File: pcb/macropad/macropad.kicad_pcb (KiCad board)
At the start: 2 copper layers, 39.5 x 62 mm, 8 parts, among them SW1 SW_Push, SW2 SW_Push, SW3 SW_Push, SW4 SW_Push, U1 XIAO-RP2040-DIP

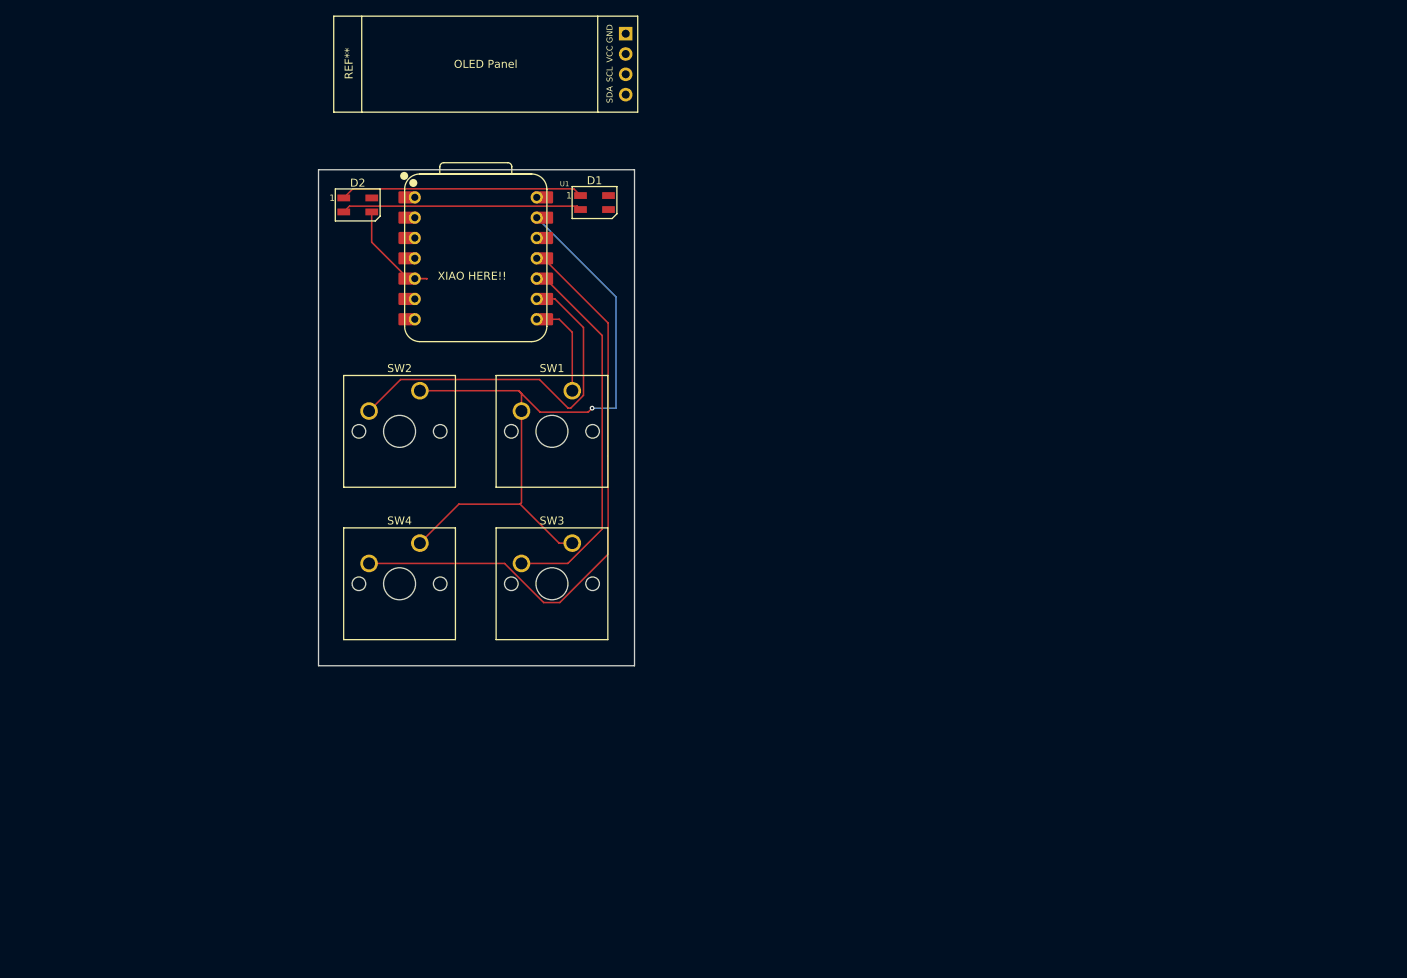
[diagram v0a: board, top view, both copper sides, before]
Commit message: changes to the pcb, case changes will follow
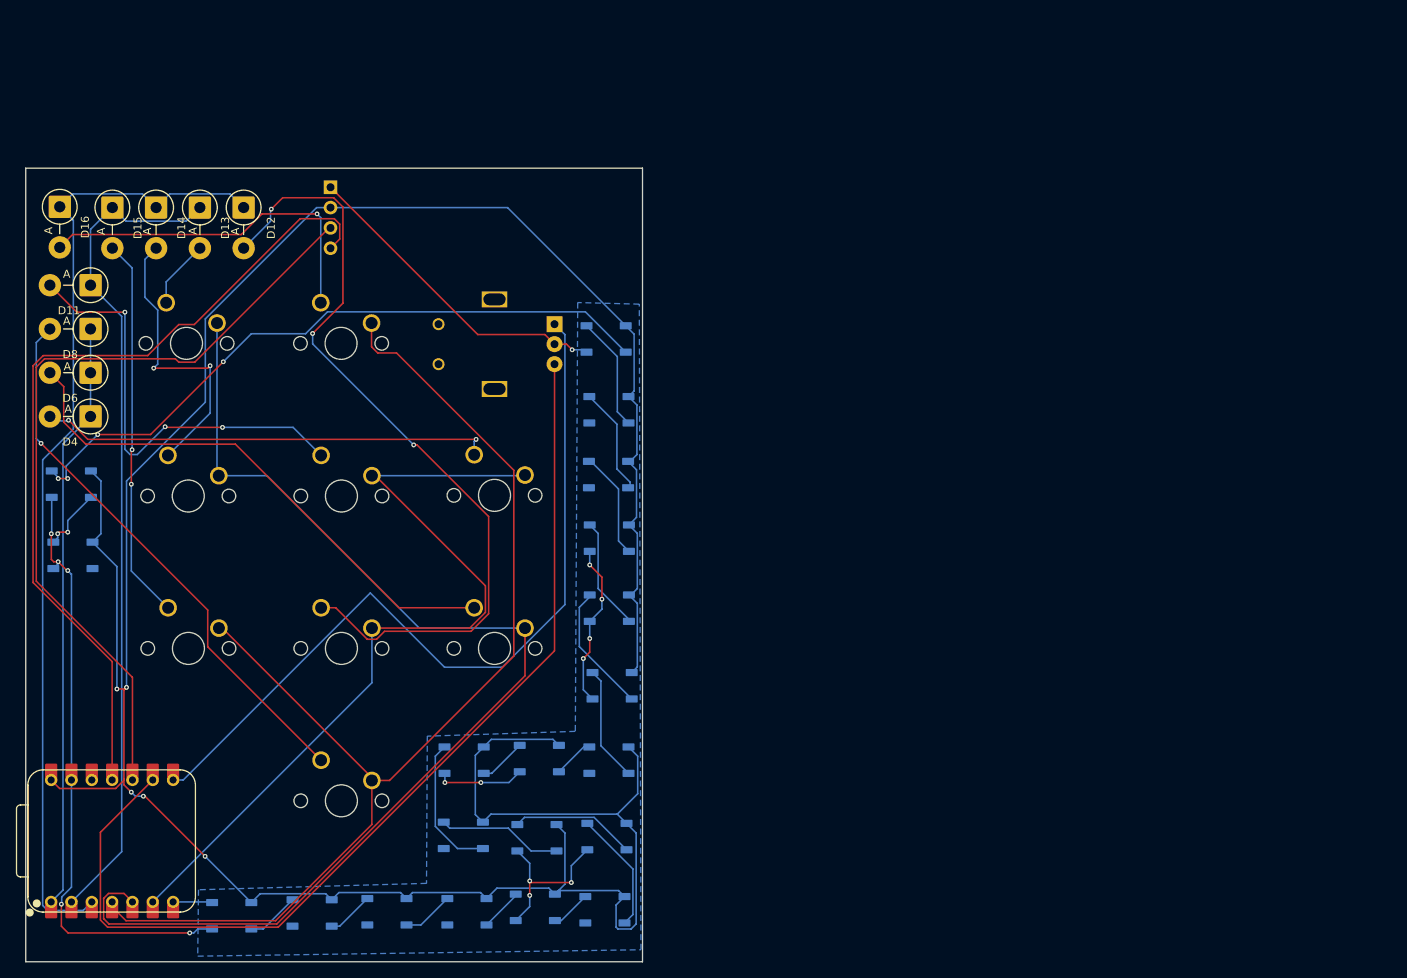
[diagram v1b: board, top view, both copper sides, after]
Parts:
- removed REF**: SSD1306-0.91-OLED-4pin-128x32, Downloads:SSD1306-0.91-OLED-4pin-128x32
- removed SW1, SW2, SW3: SW_Push, Button_Switch_Keyboard:SW_Cherry_MX_1.00u_PCB
- added D10: WS2812B, LED_SMD:LED_WS2812B_PLCC4_5.0x5.0mm_P3.2mm, B.Cu at (152.2, 110.0)
- added D11: D_Small, Diode_THT:D_5W_P5.08mm_Vertical_AnodeUp, F.Cu at (87.3, 69.6)
- added D12: D_Small, Diode_THT:D_5W_P5.08mm_Vertical_AnodeUp, F.Cu at (106.4, 59.9)
- added D13: D_Small, Diode_THT:D_5W_P5.08mm_Vertical_AnodeUp, F.Cu at (101.0, 59.9)
- added D14: D_Small, Diode_THT:D_5W_P5.08mm_Vertical_AnodeUp, F.Cu at (95.5, 59.9)
- added D15: D_Small, Diode_THT:D_5W_P5.08mm_Vertical_AnodeUp, F.Cu at (90.0, 59.9)
- added D16: D_Small, Diode_THT:D_5W_P5.08mm_Vertical_AnodeUp, F.Cu at (83.5, 59.8)
- added D17: WS2812B, LED_SMD:LED_WS2812B_PLCC4_5.0x5.0mm_P3.2mm, B.Cu at (152.2, 101.2)
- added D18: WS2812B, LED_SMD:LED_WS2812B_PLCC4_5.0x5.0mm_P3.2mm, B.Cu at (151.6, 147.7)
- added D19: WS2812B, LED_SMD:LED_WS2812B_PLCC4_5.0x5.0mm_P3.2mm, B.Cu at (152.1, 93.3)
- added D20: WS2812B, LED_SMD:LED_WS2812B_PLCC4_5.0x5.0mm_P3.2mm, B.Cu at (151.8, 138.6)
- added D21: WS2812B, LED_SMD:LED_WS2812B_PLCC4_5.0x5.0mm_P3.2mm, B.Cu at (152.1, 85.2)
- added D22: WS2812B, LED_SMD:LED_WS2812B_PLCC4_5.0x5.0mm_P3.2mm, B.Cu at (143.1, 138.7)
- added D23: WS2812B, LED_SMD:LED_WS2812B_PLCC4_5.0x5.0mm_P3.2mm, B.Cu at (151.8, 76.3)
- added D24: WS2812B, LED_SMD:LED_WS2812B_PLCC4_5.0x5.0mm_P3.2mm, B.Cu at (133.9, 138.4)
- added D25: WS2812B, LED_SMD:LED_WS2812B_PLCC4_5.0x5.0mm_P3.2mm, B.Cu at (84.9, 94.5)
- added D26: WS2812B, LED_SMD:LED_WS2812B_PLCC4_5.0x5.0mm_P3.2mm, B.Cu at (134.0, 129.0)
- added D27: WS2812B, LED_SMD:LED_WS2812B_PLCC4_5.0x5.0mm_P3.2mm, B.Cu at (143.4, 128.8)
- added D28: WS2812B, LED_SMD:LED_WS2812B_PLCC4_5.0x5.0mm_P3.2mm, B.Cu at (85.1, 103.4)
- added D29: WS2812B, LED_SMD:LED_WS2812B_PLCC4_5.0x5.0mm_P3.2mm, B.Cu at (105.0, 148.4)
- added D3: WS2812B, LED_SMD:LED_WS2812B_PLCC4_5.0x5.0mm_P3.2mm, B.Cu at (134.3, 147.9)
- added D4: D_Small, Diode_THT:D_5W_P5.08mm_Vertical_AnodeUp, F.Cu at (87.3, 86.0)
- added D5: WS2812B, LED_SMD:LED_WS2812B_PLCC4_5.0x5.0mm_P3.2mm, B.Cu at (142.9, 147.4)
- added D6: D_Small, Diode_THT:D_5W_P5.08mm_Vertical_AnodeUp, F.Cu at (87.3, 80.6)
- added D7: WS2812B, LED_SMD:LED_WS2812B_PLCC4_5.0x5.0mm_P3.2mm, B.Cu at (152.1, 129.0)
- added D8: D_Small, Diode_THT:D_5W_P5.08mm_Vertical_AnodeUp, F.Cu at (87.3, 75.1)
- added D9: WS2812B, LED_SMD:LED_WS2812B_PLCC4_5.0x5.0mm_P3.2mm, B.Cu at (152.5, 119.7)
- added OLED1: ~, Downloads:SSD1306-0.91-OLED-4pin-128x32, B.Cu at (153.8, 55.2)
- added SW11: SW_Push, Button_Switch_Keyboard:SW_Cherry_MX_1.00u_PCB, B.Cu at (116.1, 90.9)
- added SW12: SW_Push, Button_Switch_Keyboard:SW_Cherry_MX_1.00u_PCB, B.Cu at (116.1, 110.0)
- added SW13: SW_Push, Button_Switch_Keyboard:SW_Cherry_MX_1.00u_PCB, B.Cu at (96.8, 71.8)
- added SW14: SW_Push, Button_Switch_Keyboard:SW_Cherry_MX_1.00u_PCB, B.Cu at (97.0, 90.9)
- added SW15: SW_Push, Button_Switch_Keyboard:SW_Cherry_MX_1.00u_PCB, B.Cu at (97.0, 110.0)
- added SW16: SW_Push, Button_Switch_Keyboard:SW_Cherry_MX_1.00u_PCB, B.Cu at (116.1, 71.8)
- added SW17: RotaryEncoder, Downloads:RotaryEncoder_Alps_EC11E_Vertical_H20mm, B.Cu at (145.3, 74.5)
- added SW6: SW_Push, Button_Switch_Keyboard:SW_Cherry_MX_1.00u_PCB, B.Cu at (135.3, 110.0)
- added SW8: SW_Push, Button_Switch_Keyboard:SW_Cherry_MX_1.00u_PCB, B.Cu at (116.1, 129.0)
- D1, D2: value SK6812MINI -> WS2812B; footprint LED_SMD:LED_SK6812MINI_PLCC4_3.5x3.5mm_P1.75mm -> LED_SMD:LED_WS2812B_PLCC4_5.0x5.0mm_P3.2mm; moved to B.Cu
- SW4: moved to B.Cu
- moved D1 95.6 mm to (115.0, 148.1), turned to 180 degrees
- moved D2 88.4 mm to (124.3, 147.9), turned to 180 degrees
- moved U1 85.9 mm to (90.0, 139.1), turned to 90 degrees
- moved SW4 13.0 mm to (135.3, 90.8), turned to 180 degrees
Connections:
- D1 pad 1: Net-(D1-DOUT) -> VCC
- D1 pad 2: Net-(D1-VSS) -> Net-(D1-DOUT)
- D1 pad 3: unconnected-(D1-DIN-Pad3) -> GND
- D1 pad 4: +5V -> Net-(D1-DIN)
- D2 pad 1: Net-(D1-DOUT) -> VCC
- D2 pad 2: Net-(D1-VSS) -> Net-(D2-DOUT)
- D2 pad 3: Net-(D2-DIN) -> GND
- D2 pad 4: +5V -> Net-(D1-DOUT)
- SW4 pad 1: GND -> Net-(D4-A)
- SW4 pad 2: Net-(U1-GPIO3/MOSI) -> COL2
- U1 pad 1: unconnected-(U1-GPIO26/ADC0/A0-Pad1) -> ROW0
- U1 pad 11: Net-(U1-GPIO3/MOSI) -> Net-(OLED1-SDA)
- U1 pad 14: +5V -> VCC
- U1 pad 2: unconnected-(U1-GPIO27/ADC1/A1-Pad2) -> ROW1
- U1 pad 3: unconnected-(U1-GPIO28/ADC2/A2-Pad3) -> ROW2
- U1 pad 4: unconnected-(U1-GPIO29/ADC3/A3-Pad4) -> COL0
- U1 pad 5: Net-(D2-DIN) -> COL1
- U1 pad 6: unconnected-(U1-GPIO7/SCL-Pad6) -> COL2
- U1 pad 7: unconnected-(U1-GPIO0/TX-Pad7) -> Net-(D29-DIN)
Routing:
- net VCC: track 0.00 -> 365.9 mm, vias 0 -> 5
- net COL0: track 0.00 -> 146.1 mm
- net COL1: track 0.00 -> 143.9 mm
- net ROW2: track 0.00 -> 122.2 mm
- net Net-(OLED1-SDA): track 0.00 -> 105.6 mm
- net ROW1: track 0.00 -> 104.5 mm
- net COL2: track 0.00 -> 103.0 mm
- net Net-(D12-A): track 0.00 -> 102.2 mm, vias 0 -> 3
- net Net-(U1-GPIO1/RX): track 12.4 -> 101.3 mm
- net Net-(D23-DOUT): track 0.00 -> 84.1 mm, vias 0 -> 4
- net Net-(U1-GPIO2/SCK): track 46.4 -> 127.5 mm
- net GND: track 91.5 -> 168.5 mm, vias 1 -> 15
- net Net-(U1-GPIO3/MOSI): track 75.6 -> 0.00 mm
- net ROW0: track 0.00 -> 73.7 mm
- net Net-(D8-A): track 0.00 -> 69.4 mm, vias 0 -> 1
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- added copper zone on B.Cu, net GND
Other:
- board size 39.5 x 62 mm -> 77.1 x 99.2 mm
- board text removed: "Itay Zimet's Hackpad"
- board text removed: "XIAO HERE!!"

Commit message: remade pcb
removed leds and better wiring (much better)
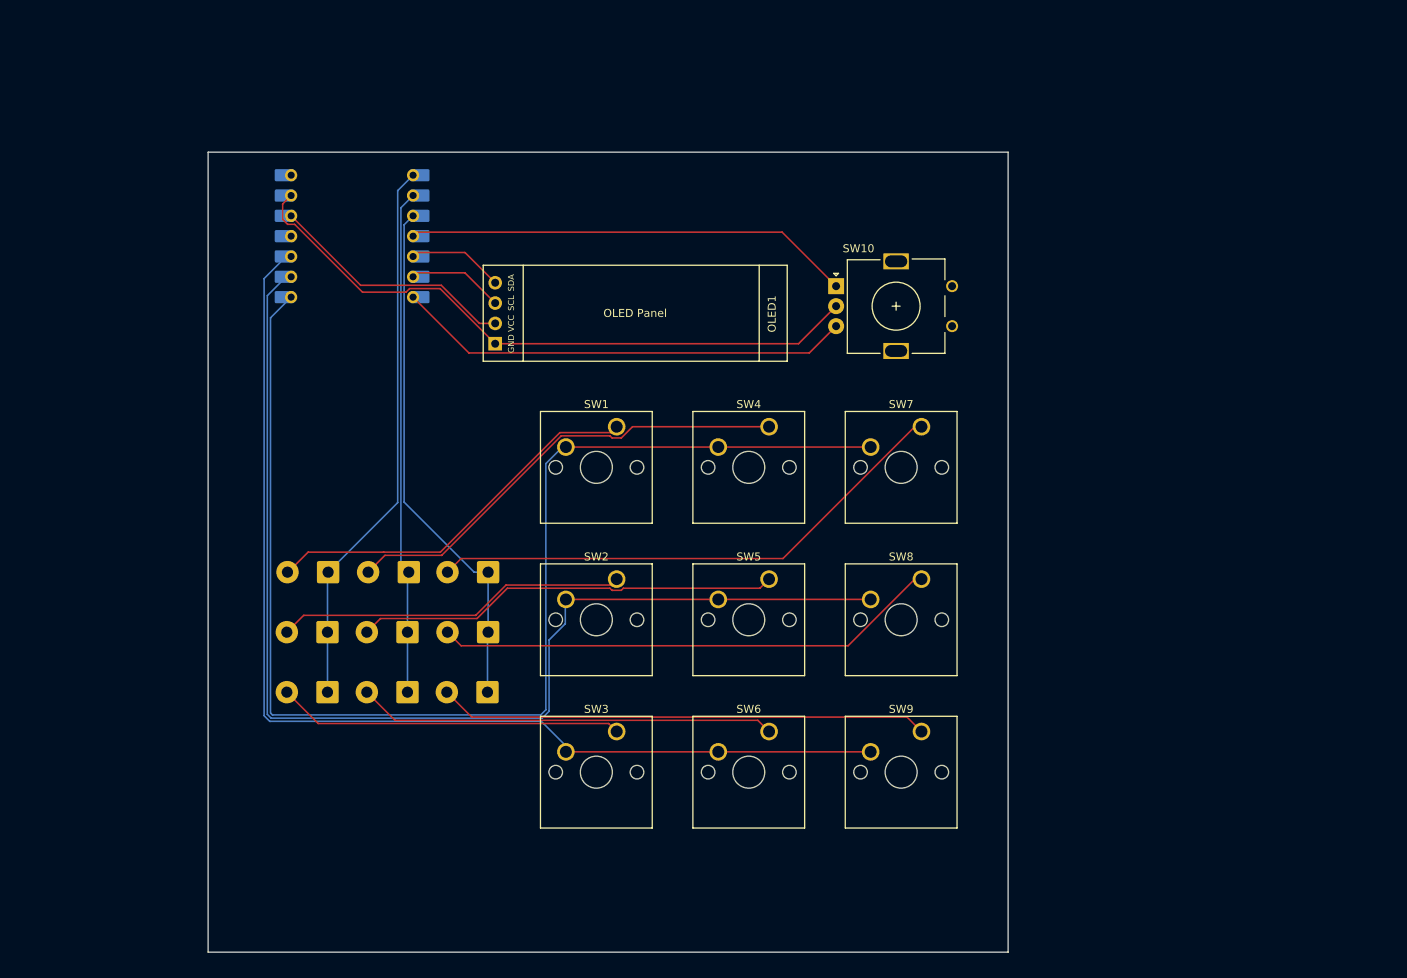
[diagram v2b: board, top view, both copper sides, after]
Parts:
- removed D10, D17, D18, D19, D20, D21, D22, D23, D24, D25, D26, D27, D28, D29: WS2812B, LED_SMD:LED_WS2812B_PLCC4_5.0x5.0mm_P3.2mm
- removed D11, D12, D13, D14, D15, D16: D_Small, Diode_THT:D_5W_P5.08mm_Vertical_AnodeUp
- removed SW11, SW12, SW13, SW14, SW15, SW16: SW_Push, Button_Switch_Keyboard:SW_Cherry_MX_1.00u_PCB
- removed SW17: RotaryEncoder, Downloads:RotaryEncoder_Alps_EC11E_Vertical_H20mm
- added SW1: SW_Push, Library:SW_Cherry_MX_1.00u_PCB, F.Cu at (153.1, 87.3)
- added SW10: RotaryEncoder, Downloads:RotaryEncoder_Alps_EC11E_Vertical_H20mm, F.Cu at (180.5, 69.8)
- added SW2: SW_Push, Library:SW_Cherry_MX_1.00u_PCB, F.Cu at (153.1, 106.4)
- added SW3: SW_Push, Library:SW_Cherry_MX_1.00u_PCB, F.Cu at (153.1, 125.4)
- added SW5: SW_Push, Library:SW_Cherry_MX_1.00u_PCB, F.Cu at (172.1, 106.4)
- added SW7: SW_Push, Library:SW_Cherry_MX_1.00u_PCB, F.Cu at (191.2, 87.3)
- added SW9: SW_Push, Library:SW_Cherry_MX_1.00u_PCB, F.Cu at (191.2, 125.4)
- D1, D2, D3, D5, D7, D9: value WS2812B -> D_Small; footprint LED_SMD:LED_WS2812B_PLCC4_5.0x5.0mm_P3.2mm -> Diode_THT:D_5W_P5.08mm_Vertical_AnodeUp
- D4, D6, D8, U1: moved to B.Cu
- OLED1: moved to F.Cu
- SW4, SW6, SW8: footprint Button_Switch_Keyboard:SW_Cherry_MX_1.00u_PCB -> Library:SW_Cherry_MX_1.00u_PCB; moved to F.Cu
- moved U1 81.3 mm to (120.0, 63.5), turned to 180 degrees
- moved SW8 78.4 mm to (191.2, 106.4), turned to 0 degrees
- moved D8 62.5 mm to (137.0, 113.0)
- moved D6 56.3 mm to (126.9, 120.5)
- moved D4 44.3 mm to (127.1, 105.5)
- moved D1 42.6 mm to (117.0, 105.5)
- moved SW6 40.0 mm to (172.1, 125.4), turned to 0 degrees
- moved D5 37.9 mm to (126.9, 113.0)
- moved SW4 37.0 mm to (172.1, 87.3), turned to 0 degrees
- moved D2 35.7 mm to (116.9, 113.0)
- moved D3 32.5 mm to (116.9, 120.5)
- moved OLED1 31.6 mm to (174.4, 79.1)
- moved D7 27.9 mm to (137.0, 105.5)
- moved D9 15.6 mm to (136.9, 120.5)
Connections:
- D1 pad 1: VCC -> ROW0
- D1 pad 2: Net-(D1-DOUT) -> Net-(D1-A)
- D2 pad 1: VCC -> ROW0
- D2 pad 2: Net-(D2-DOUT) -> Net-(D2-A)
- D3 pad 1: VCC -> ROW0
- D3 pad 2: Net-(D3-DOUT) -> Net-(D3-A)
- D4 pad 1: ROW0 -> ROW1
- D5 pad 1: VCC -> ROW1
- D6 pad 1: ROW0 -> ROW1
- D7 pad 1: VCC -> ROW2
- D7 pad 2: Net-(D7-DOUT) -> Net-(D7-A)
- D8 pad 1: ROW0 -> ROW2
- D9 pad 1: VCC -> ROW2
- OLED1 pad 2: VCC -> VCCQ
- OLED1 pad 3: Net-(OLED1-SCL) -> OLED_SCL
- OLED1 pad 4: Net-(OLED1-SDA) -> OLED_SDA
- SW6 pad 2: COL1 -> COL0
- SW8 pad 2: COL0 -> COL1
- U1 pad 10: Net-(OLED1-SCL) -> COL0
- U1 pad 11: Net-(OLED1-SDA) -> LED_CNTRL
- U1 pad 12: unconnected-(U1-3V3-Pad12) -> VCCQ
- U1 pad 4: COL0 -> EC11_A
- U1 pad 5: COL1 -> OLED_SDA
- U1 pad 6: COL2 -> OLED_SCL
- U1 pad 7: Net-(D29-DIN) -> EC11_B
- U1 pad 8: Net-(U1-GPIO1/RX) -> COL2
- U1 pad 9: Net-(U1-GPIO2/SCK) -> COL1
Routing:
- net VCC: track 365.9 -> 0.00 mm, vias 5 -> 0
- net Net-(U1-GPIO2/SCK): track 127.5 -> 0.00 mm
- net Net-(OLED1-SDA): track 105.6 -> 0.00 mm
- net Net-(D12-A): track 102.2 -> 0.00 mm, vias 3 -> 0
- net Net-(U1-GPIO1/RX): track 101.3 -> 0.00 mm
- net Net-(OLED1-SCL): track 100.9 -> 0.00 mm
- net GND: track 168.5 -> 81.4 mm, vias 15 -> 0
- net Net-(D23-DOUT): track 84.1 -> 0.00 mm, vias 4 -> 0
- net Net-(D7-A): track 0.00 -> 65.9 mm
- net EC11_B: track 0.00 -> 57.2 mm
- net ROW2: track 122.2 -> 65.3 mm
- net COL2: track 103.0 -> 159.6 mm
- net EC11_A: track 0.00 -> 55.9 mm
- net Net-(D11-A): track 55.6 -> 0.00 mm, vias 3 -> 0
- net Net-(D1-A): track 0.00 -> 48.6 mm
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- removed copper zone on B.Cu, net GND
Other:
- board size 77.1 x 99.2 mm -> 100 x 100 mm
